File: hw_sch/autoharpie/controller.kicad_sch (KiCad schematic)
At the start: 1 part, among them U1 Teensy4.1

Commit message: isolated ground
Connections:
- net GND: now also U1.1 (GND), U1.34 (GND), U1.47 (GND), U1.52 (GND), U1.58 (GND), U1.59 (GND)
- net USB_D+: now also U1.57 (D+)
- net USB_D-: now also U1.56 (D-)
- net VBUS: now also U1.55 (5V)
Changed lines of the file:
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@@
 (kicad_sch (version 20230121) (generator eeschema)
   (paper "A4")
+  (junction (at 165.1 140.97) (diameter 0) (color 0 0 0 0)
+  )
+  (wire (pts (xy 151.13 127) (xy 151.13 130.81))
+    (stroke (width 0) (type default))
+  )
   (wire (pts (xy 233.68 57.15) (xy 227.33 57.15))
     (stroke (width 0) (type default))
   )
+  (wire (pts (xy 165.1 140.97) (xy 171.45 140.97))
+    (stroke (width 0) (type default))
+  )
+  (wire (pts (xy 165.1 135.89) (xy 171.45 135.89))
+    (stroke (width 0) (type default))
+  )
+  (wire (pts (xy 199.39 148.59) (xy 199.39 157.48))
+    (stroke (width 0) (type default))
+  )
   (wire (pts (xy 233.68 52.07) (xy 233.68 57.15))
     (stroke (width 0) (type default))
   )
+  (wire (pts (xy 165.1 133.35) (xy 171.45 133.35))
+    (stroke (width 0) (type default))
+  )
+  (wire (pts (xy 227.33 63.5) (xy 237.49 63.5))
+    (stroke (width 0) (type default))
+  )
+  (wire (pts (xy 165.1 138.43) (xy 165.1 140.97))
+    (stroke (width 0) (type default))
+  )
+  (wire (pts (xy 227.33 96.52) (xy 237.49 96.52))
+    (stroke (width 0) (type default))
+  )
+  (wire (pts (xy 171.45 130.81) (xy 151.13 130.81))
+    (stroke (width 0) (type default))
+  )
   (wire (pts (xy 165.1 124.46) (xy 171.45 124.46))
     (stroke (width 0) (type default))
   )
+  (wire (pts (xy 171.45 138.43) (xy 165.1 138.43))
+    (stroke (width 0) (type default))
+  )
   (wire (pts (xy 172.72 180.34) (xy 172.72 190.5))
     (stroke (width 0) (type default))
@@
     (stroke (width 0) (type default))
   )
+  (wire (pts (xy 171.45 60.96) (xy 161.29 60.96))
+    (stroke (width 0) (type default))
+  )
   (wire (pts (xy 165.1 127) (xy 171.45 127))
+    (stroke (width 0) (type default))
+  )
+  (wire (pts (xy 165.1 140.97) (xy 165.1 143.51))
     (stroke (width 0) (type default))
   )
@@
     (effects (font (size 1.27 1.27)) (justify left bottom))
   )
+  (label "MCU_GND" (at 199.39 157.48 90) (fields_autoplaced)
+    (effects (font (size 1.27 1.27)) (justify left bottom))
+  )
+  (label "MCU_GND" (at 237.49 63.5 180) (fields_autoplaced)
+    (effects (font (size 1.27 1.27)) (justify right bottom))
+  )
+  (label "MCU_GND" (at 161.29 60.96 0) (fields_autoplaced)
+    (effects (font (size 1.27 1.27)) (justify left bottom))
+  )
+  (label "MCU_GND" (at 237.49 96.52 180) (fields_autoplaced)
+    (effects (font (size 1.27 1.27)) (justify right bottom))
+  )
+  (hierarchical_label "USB_D-" (shape bidirectional) (at 165.1 133.35 180) (fields_autoplaced)
+    (effects (font (size 1.27 1.27)) (justify right))
+  )
   (hierarchical_label "USB_D-" (shape bidirectional) (at 165.1 124.46 180) (fields_autoplaced)
     (effects (font (size 1.27 1.27)) (justify right))
   )
   (hierarchical_label "USB_D+" (shape bidirectional) (at 165.1 127 180) (fields_autoplaced)
+    (effects (font (size 1.27 1.27)) (justify right))
+  )
+  (hierarchical_label "USB_D+" (shape bidirectional) (at 165.1 135.89 180) (fields_autoplaced)
     (effects (font (size 1.27 1.27)) (justify right))
   )
@@
     )
   )
+  (symbol (lib_id "power:VBUS") (at 151.13 127 0) (unit 1)
+    (in_bom yes) (on_board yes) (dnp no) (fields_autoplaced)
+    (property "Reference" "#PWR0120" (at 151.13 130.81 0)
+      (effects (font (size 1.27 1.27)) hide)
+    )
+    (property "Value" "VBUS" (at 151.13 123.19 0)
+      (effects (font (size 1.27 1.27)))
+    )
+    (property "Footprint" "" (at 151.13 127 0)
+      (effects (font (size 1.27 1.27)) hide)
+    )
+    (property "Datasheet" "" (at 151.13 127 0)
+      (effects (font (size 1.27 1.27)) hide)
+    )
+    (pin "1")
+    (instances
+      (project "autoharpie"
+        (path "/f22a88c4-866b-40a0-9fc2-96344be0ec71/4d9f1d6c-21ab-45cf-b058-d32e1eb1198b"
+          (reference "#PWR0120") (unit 1)
+        )
+      )
+    )
+  )
   (symbol (lib_id "power:VBUS") (at 233.68 52.07 0) (unit 1)
     (in_bom yes) (on_board yes) (dnp no) (fields_autoplaced)
@@
         )
       )
+    )
+  )
+  (symbol (lib_id "power:GND") (at 165.1 143.51 0) (unit 1)
+    (in_bom yes) (on_board yes) (dnp no) (fields_autoplaced)
+    (property "Reference" "#PWR0121" (at 165.1 149.86 0)
+      (effects (font (size 1.27 1.27)) hide)
+    )
+    (property "Value" "GND" (at 165.1 148.59 0)
+      (effects (font (size 1.27 1.27)))
+    )
+    (property "Footprint" "" (at 165.1 143.51 0)
+      (effects (font (size 1.27 1.27)) hide)
+    )
+    (property "Datasheet" "" (at 165.1 143.51 0)
+      (effects (font (size 1.27 1.27)) hide)
+    )
+    (pin "1")
+    (instances
+      (project "autoharpie"
+        (path "/f22a88c4-866b-40a0-9fc2-96344be0ec71/4d9f1d6c-21ab-45cf-b058-d32e1eb1198b"
+          (reference "#PWR0121") (unit 1)
+        )
+      )

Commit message: stm32
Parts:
- removed U1: Teensy4.1, symbol teensy:Teensy4.1
- added C1, C2, C3, C4, C48, C49, C5, C50, C9: 0.1u, symbol Device:C
- added C46, C47: 1u, symbol Device:C
- added C6: 4.7u, symbol Device:C
- added C7, C8: 2.2u, symbol Device:C
- added FB1: FerriteBead_Small, symbol Device:FerriteBead_Small
- added J6: Conn_01x02_Pin, Connector:JWT_A3963_1x02_P3.96mm_Vertical, symbol Connector:Conn_01x02_Pin
- added R16: 10k, symbol Device:R
- added R3: 47, symbol Device:R
- added SW3, SW4: SW_Push, symbol Switch:SW_Push
- added U1: STM32H7A3VITx, Package_QFP:LQFP-100_14x14mm_P0.5mm, symbol MCU_ST_STM32H7:STM32H7A3VITx
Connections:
- net GND: now also C1.2, C2.2, C3.2, C4.2, C46.2, C47.2, C48.2, C49.2, C5.2, C50.2, C6.2, C7.2, C8.2, C9.2, R16.2, SW4.1, U1.10 (VSS), U1.19 (VSSA), U1.26 (VSS), U1.49 (VSS), U1.74 (VSS), U1.99 (VSS)
- new net +3V3: C1.1, C2.1, C3.1, C4.1, C5.1, C6.1, FB1.1, SW3.2, U1.100 (VDD), U1.11 (VDD), U1.27 (VDD), U1.50 (VDD), U1.75 (VDD)
- new net BOOT: C49.1, R16.1, SW3.1, U1.94 (BOOT0)
- new net RESET: C50.1, SW4.2, U1.14 (NRST)
- new net SWCLK: J6.2 (Pin_2), U1.76 (PA14)
- new net SWDIO: J6.1 (Pin_1), U1.72 (PA13)
- new net VADD: C46.1, C9.1, FB1.2, R3.1, U1.21 (VDDA)
- new net VCAP0: C7.1, U1.48 (VCAP)
- new net VCAP1: C8.1, U1.73 (VCAP)
- new net VREF: C47.1, C48.1, R3.2, U1.20 (VREF+)

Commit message: DAC, touch sensors
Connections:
- net VBUS: now reaches U1.68 (PA9)
- net USB_ID: now reaches U1.69 (PA10)
- net USB_D-: now reaches U1.70 (PA11)
- net USD_D+: now reaches U1.71 (PA12)
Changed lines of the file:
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@@
+    (stroke (width 0) (type default))
+  )
+  (wire (pts (xy 125.73 63.5) (xy 130.81 63.5))
     (stroke (width 0) (type default))
   )
@@
     (stroke (width 0) (type default))
   )
+  (wire (pts (xy 125.73 66.04) (xy 130.81 66.04))
+    (stroke (width 0) (type default))
+  )
   (wire (pts (xy 262.89 64.77) (xy 274.32 64.77))
     (stroke (width 0) (type default))
@@
   )
   (wire (pts (xy 125.73 68.58) (xy 149.86 68.58))
+    (stroke (width 0) (type default))
+  )
+  (wire (pts (xy 125.73 60.96) (xy 130.81 60.96))
     (stroke (width 0) (type default))
   )
@@
   (label "SWDIO" (at 148.59 68.58 180) (fields_autoplaced)
     (effects (font (size 1.27 1.27)) (justify right bottom))
+  )
+  (hierarchical_label "USD_D+" (shape input) (at 130.81 66.04 0) (fields_autoplaced)
+    (effects (font (size 1.27 1.27)) (justify left))
+  )
+  (hierarchical_label "USB_ID" (shape input) (at 130.81 60.96 0) (fields_autoplaced)
+    (effects (font (size 1.27 1.27)) (justify left))
+  )
+  (hierarchical_label "USB_D-" (shape input) (at 130.81 63.5 0) (fields_autoplaced)
+    (effects (font (size 1.27 1.27)) (justify left))
   )
   (symbol (lib_id "Device:R") (at 209.55 101.6 0) (unit 1)
@@
         )
       )
+    )
+  )
+  (symbol (lib_id "power:VBUS") (at 125.73 58.42 270) (unit 1)
+    (in_bom yes) (on_board yes) (dnp no) (fields_autoplaced)
+    (property "Reference" "#PWR0174" (at 121.92 58.42 0)
+      (effects (font (size 1.27 1.27)) hide)
+    )
+    (property "Value" "VBUS" (at 129.54 59.055 90)
+      (effects (font (size 1.27 1.27)) (justify left))
+    )
+    (property "Footprint" "" (at 125.73 58.42 0)
+      (effects (font (size 1.27 1.27)) hide)
+    )
+    (property "Datasheet" "" (at 125.73 58.42 0)
+      (effects (font (size 1.27 1.27)) hide)
+    )
+    (pin "1")
+    (instances
+      (project "autoharpie"
+        (path "/f22a88c4-866b-40a0-9fc2-96344be0ec71/4d9f1d6c-21ab-45cf-b058-d32e1eb1198b"
+          (reference "#PWR0174") (unit 1)
+        )
+      )

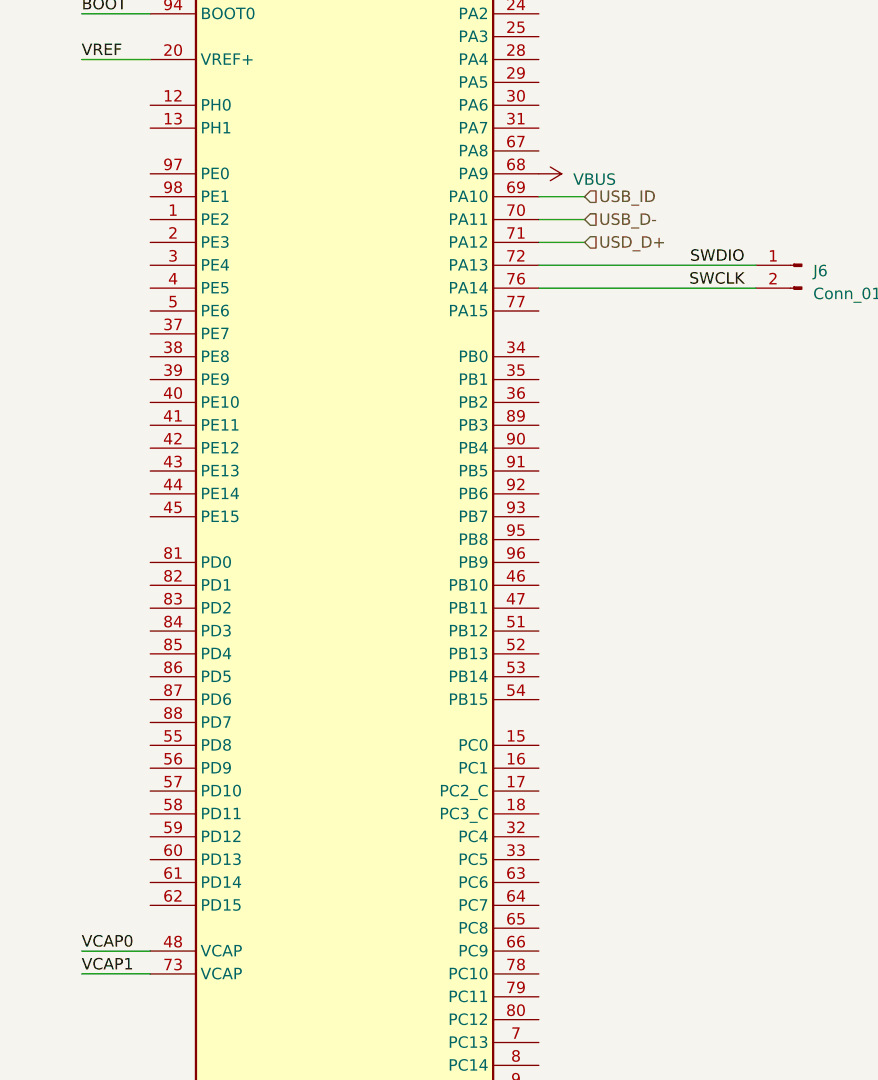
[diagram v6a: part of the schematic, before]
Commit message: DAC wiring, add heirch pins
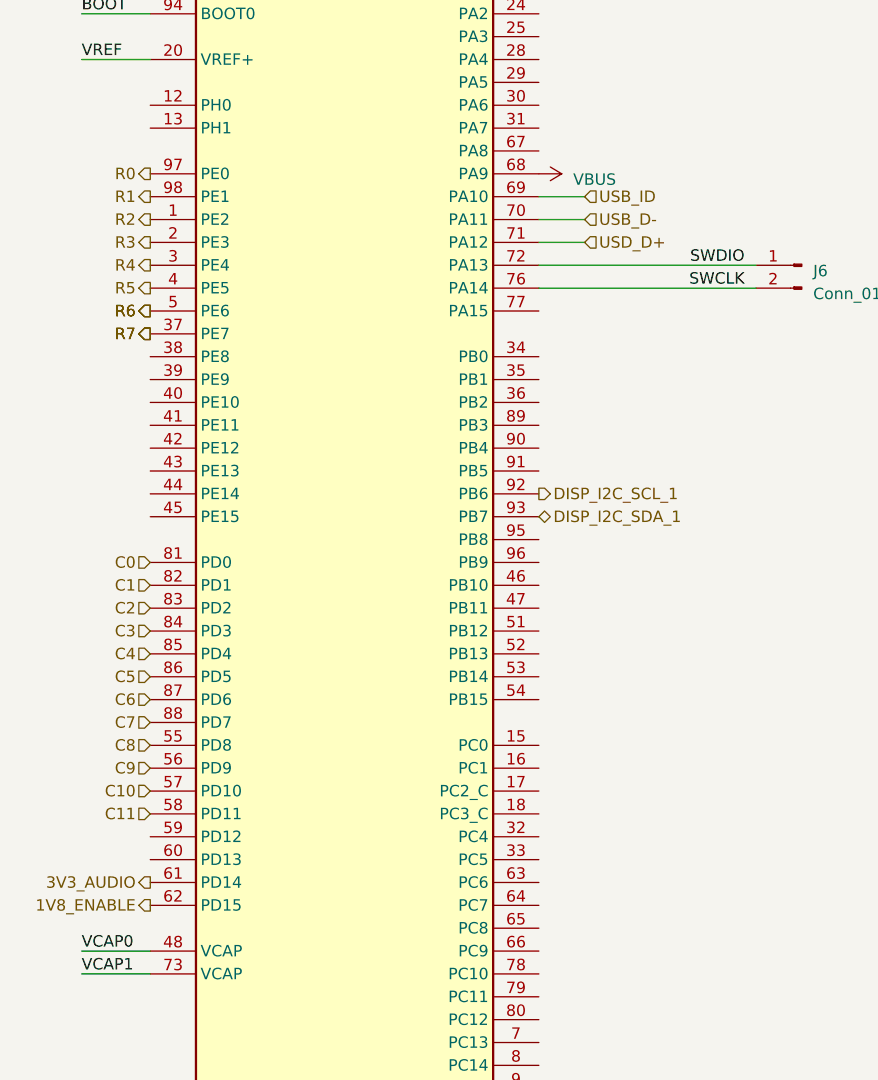
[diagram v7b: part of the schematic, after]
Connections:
- net R2: now reaches U1.1 (PE2)
- net R3: now reaches U1.2 (PE3)
- net R4: now reaches U1.3 (PE4)
- net R7: now reaches U1.37 (PE7)
- net R5: now reaches U1.4 (PE5)
- net R6: now reaches U1.5 (PE6)
- net C8: now reaches U1.55 (PD8)
- net C9: now reaches U1.56 (PD9)
- net C10: now reaches U1.57 (PD10)
- net C11: now reaches U1.58 (PD11)
- net 3V3_AUDIO: now reaches U1.61 (PD14)
- net 1V8_ENABLE: now reaches U1.62 (PD15)
- net C0: now reaches U1.81 (PD0)
- net C1: now reaches U1.82 (PD1)
- net C2: now reaches U1.83 (PD2)
- net C3: now reaches U1.84 (PD3)
- net C4: now reaches U1.85 (PD4)
- net C5: now reaches U1.86 (PD5)
- net C6: now reaches U1.87 (PD6)
- net C7: now reaches U1.88 (PD7)
- net DISP_I2C_SCL_1: now reaches U1.92 (PB6)
- net DISP_I2C_SDA_1: now reaches U1.93 (PB7)
- net R0: now reaches U1.97 (PE0)
- net R1: now reaches U1.98 (PE1)
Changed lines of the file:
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@@
     (effects (font (size 1.27 1.27)) (justify right bottom))
+  )
+  (hierarchical_label "R6" (shape output) (at 82.55 73.66 180) (fields_autoplaced)
+    (effects (font (size 1.27 1.27)) (justify right))
+  )
+  (hierarchical_label "DISP_I2C_SDA_1" (shape bidirectional) (at 125.73 96.52 0) (fields_autoplaced)
+    (effects (font (size 1.27 1.27)) (justify left))
+  )
+  (hierarchical_label "R5" (shape output) (at 82.55 71.12 180) (fields_autoplaced)
+    (effects (font (size 1.27 1.27)) (justify right))
+  )
+  (hierarchical_label "C3" (shape input) (at 82.55 109.22 180) (fields_autoplaced)
+    (effects (font (size 1.27 1.27)) (justify right))
+  )
+  (hierarchical_label "R6" (shape output) (at 82.55 73.66 180) (fields_autoplaced)
+    (effects (font (size 1.27 1.27)) (justify right))
+  )
+  (hierarchical_label "R1" (shape output) (at 82.55 60.96 180) (fields_autoplaced)
+    (effects (font (size 1.27 1.27)) (justify right))
+  )
+  (hierarchical_label "C1" (shape input) (at 82.55 104.14 180) (fields_autoplaced)
+    (effects (font (size 1.27 1.27)) (justify right))
+  )
+  (hierarchical_label "R4" (shape output) (at 82.55 68.58 180) (fields_autoplaced)
+    (effects (font (size 1.27 1.27)) (justify right))
+  )
+  (hierarchical_label "R0" (shape output) (at 82.55 58.42 180) (fields_autoplaced)
+    (effects (font (size 1.27 1.27)) (justify right))
   )
   (hierarchical_label "USD_D+" (shape input) (at 130.81 66.04 0) (fields_autoplaced)
     (effects (font (size 1.27 1.27)) (justify left))
   )
+  (hierarchical_label "C10" (shape input) (at 82.55 127 180) (fields_autoplaced)
+    (effects (font (size 1.27 1.27)) (justify right))
+  )
   (hierarchical_label "USB_ID" (shape input) (at 130.81 60.96 0) (fields_autoplaced)
     (effects (font (size 1.27 1.27)) (justify left))
+  )
+  (hierarchical_label "C9" (shape input) (at 82.55 124.46 180) (fields_autoplaced)
+    (effects (font (size 1.27 1.27)) (justify right))
+  )
+  (hierarchical_label "R3" (shape output) (at 82.55 66.04 180) (fields_autoplaced)
+    (effects (font (size 1.27 1.27)) (justify right))
+  )
+  (hierarchical_label "1V8_ENABLE" (shape output) (at 82.55 139.7 180) (fields_autoplaced)
+    (effects (font (size 1.27 1.27)) (justify right))
   )
   (hierarchical_label "USB_D-" (shape input) (at 130.81 63.5 0) (fields_autoplaced)
     (effects (font (size 1.27 1.27)) (justify left))
   )
+  (hierarchical_label "C11" (shape input) (at 82.55 129.54 180) (fields_autoplaced)
+    (effects (font (size 1.27 1.27)) (justify right))
+  )
+  (hierarchical_label "C2" (shape input) (at 82.55 106.68 180) (fields_autoplaced)
+    (effects (font (size 1.27 1.27)) (justify right))
+  )
+  (hierarchical_label "C6" (shape input) (at 82.55 116.84 180) (fields_autoplaced)
+    (effects (font (size 1.27 1.27)) (justify right))
+  )
+  (hierarchical_label "C0" (shape input) (at 82.55 101.6 180) (fields_autoplaced)
+    (effects (font (size 1.27 1.27)) (justify right))
+  )
+  (hierarchical_label "3V3_AUDIO" (shape output) (at 82.55 137.16 180) (fields_autoplaced)
+    (effects (font (size 1.27 1.27)) (justify right))
+  )
+  (hierarchical_label "R7" (shape output) (at 82.55 76.2 180) (fields_autoplaced)
+    (effects (font (size 1.27 1.27)) (justify right))
+  )
+  (hierarchical_label "C4" (shape input) (at 82.55 111.76 180) (fields_autoplaced)
+    (effects (font (size 1.27 1.27)) (justify right))
+  )
+  (hierarchical_label "C8" (shape input) (at 82.55 121.92 180) (fields_autoplaced)
+    (effects (font (size 1.27 1.27)) (justify right))
+  )
+  (hierarchical_label "C7" (shape input) (at 82.55 119.38 180) (fields_autoplaced)
+    (effects (font (size 1.27 1.27)) (justify right))
+  )
+  (hierarchical_label "R7" (shape output) (at 82.55 76.2 180) (fields_autoplaced)
+    (effects (font (size 1.27 1.27)) (justify right))
+  )
+  (hierarchical_label "C5" (shape input) (at 82.55 114.3 180) (fields_autoplaced)
+    (effects (font (size 1.27 1.27)) (justify right))
+  )
+  (hierarchical_label "DISP_I2C_SCL_1" (shape output) (at 125.73 93.98 0) (fields_autoplaced)
+    (effects (font (size 1.27 1.27)) (justify left))
+  )
+  (hierarchical_label "R2" (shape output) (at 82.55 63.5 180) (fields_autoplaced)
+    (effects (font (size 1.27 1.27)) (justify right))
+  )
   (symbol (lib_id "Device:R") (at 209.55 101.6 0) (unit 1)

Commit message: finish keypad
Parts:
- removed C8: 2.2u, symbol Device:C
- removed J6: Conn_01x02_Pin, Connector:JWT_A3963_1x02_P3.96mm_Vertical, symbol Connector:Conn_01x02_Pin
- removed U1: STM32H7A3VITx, Package_QFP:LQFP-100_14x14mm_P0.5mm, symbol MCU_ST_STM32H7:STM32H7A3VITx
- added U1: STM32F446RCTx, Package_QFP:LQFP-64_10x10mm_P0.5mm, symbol MCU_ST_STM32F4:STM32F446RCTx
- C1, C2, C3, C4, C48, C5, C9: value 0.1u -> 100n
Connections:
- net BOOT: now also U1.60 (BOOT0)
- net GND: now also U1.12 (VSSA), U1.18 (VSS), U1.31 (VSS), U1.47 (VSS), U1.63 (VSS)
- net RESET: now also U1.7 (NRST)
- net VCAP0: now also U1.30 (VCAP_1)
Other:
- moved on the sheet: C46, C9
